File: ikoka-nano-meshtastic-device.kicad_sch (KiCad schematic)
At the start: 8 parts, among them J1 Battery, J2 Solar, J3 Qwiic_RA, Q1 FDN302P, U1 Seeed Studio XIAO nRF52840, U2 E22-900M30S

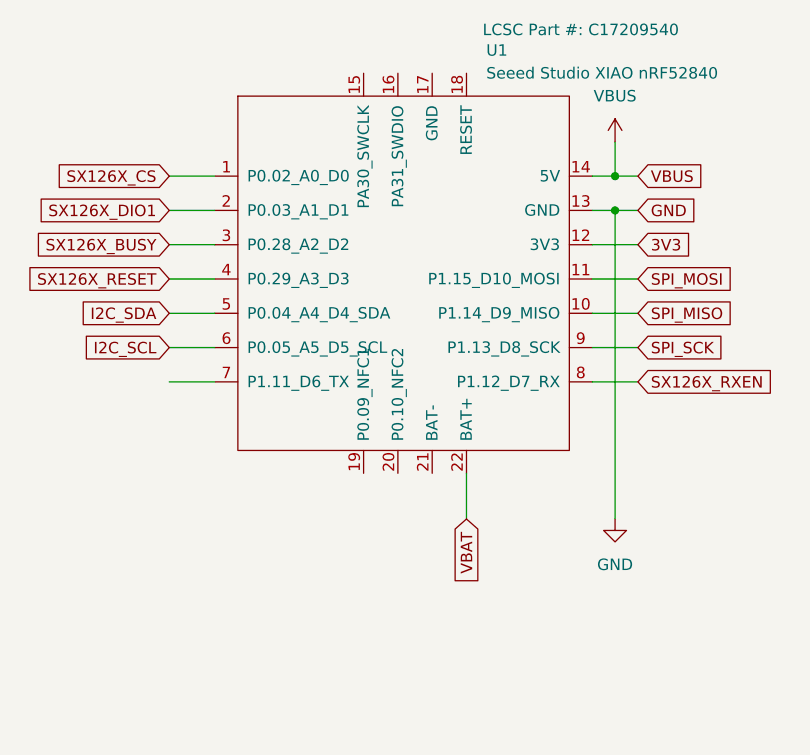
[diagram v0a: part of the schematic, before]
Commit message: Rebase XIAO BLE hand soldering symbol/footprint on upstream
Signed-off-by: Andrew Yong <me@ndoo.sg>
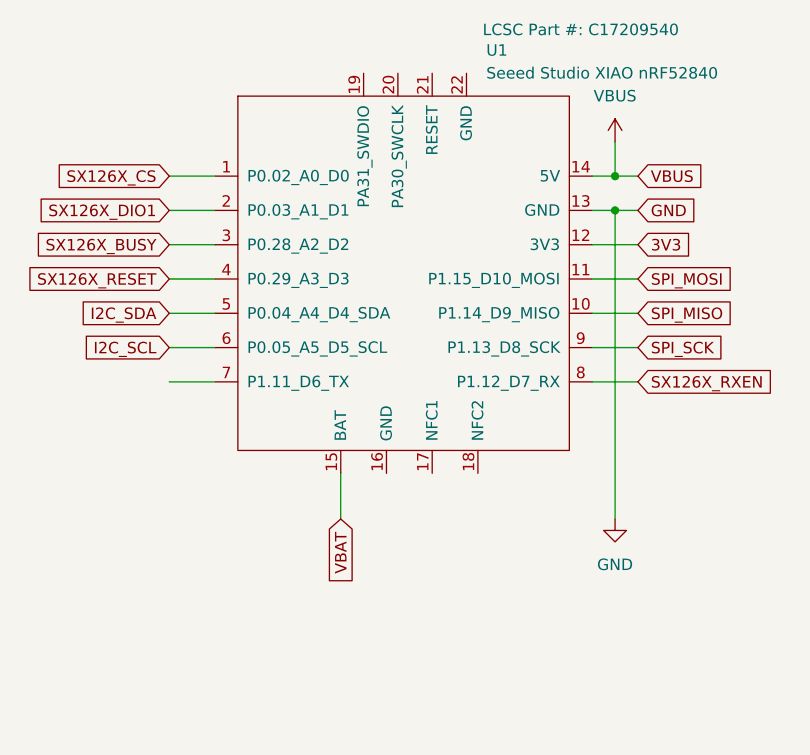
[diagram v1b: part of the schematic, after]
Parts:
- U1: footprint Seeed Studio XIAO Series Library:XIAO-nRF52840-BatteryPTH-14P-2.54-21X17.8MM -> Seeed Studio XIAO Series Library:XIAO-nRF52840-SMD_Handsoldering; symbol Seeed_Studio_XIAO_Series:Seeed Studio XIAO nRF52840 -> Seeed_Studio_XIAO_Series:XIAO-nRF52840-SMD
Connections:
- net VBAT: now also U1.15 (BAT); no longer U1.22 (BAT+)
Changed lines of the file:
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@@
 	(wire
 		(pts
-			(xy 87.63 81.28) (xy 87.63 86.36)
+			(xy 73.66 81.28) (xy 73.66 86.36)
 		)
 		(stroke
@@
 	(global_label "VBAT"
 		(shape input)
-		(at 87.63 86.36 270)
+		(at 73.66 86.36 270)
 		(fields_autoplaced yes)
 		(effects
@@
 		)
 		(property "Intersheetrefs" "${INTERSHEET_REFS}"
-			(at 87.63 93.76 90)
+			(at 73.66 93.76 90)
 			(effects
 				(font
@@
 	)
 	(symbol
-		(lib_id "Seeed_Studio_XIAO_Series:Seeed Studio XIAO nRF52840")
+		(lib_id "Seeed_Studio_XIAO_Series:XIAO-nRF52840-SMD")
 		(at 81.28 59.69 0)
 		(unit 1)
@@
 			)
 		)
-		(property "Footprint" "Seeed Studio XIAO Series Library:XIAO-nRF52840-BatteryPTH-14P-2.54-21X17.8MM"
+		(property "Footprint" "Seeed Studio XIAO Series Library:XIAO-nRF52840-SMD_Handsoldering"
 			(at 72.39 54.61 0)
 			(effects

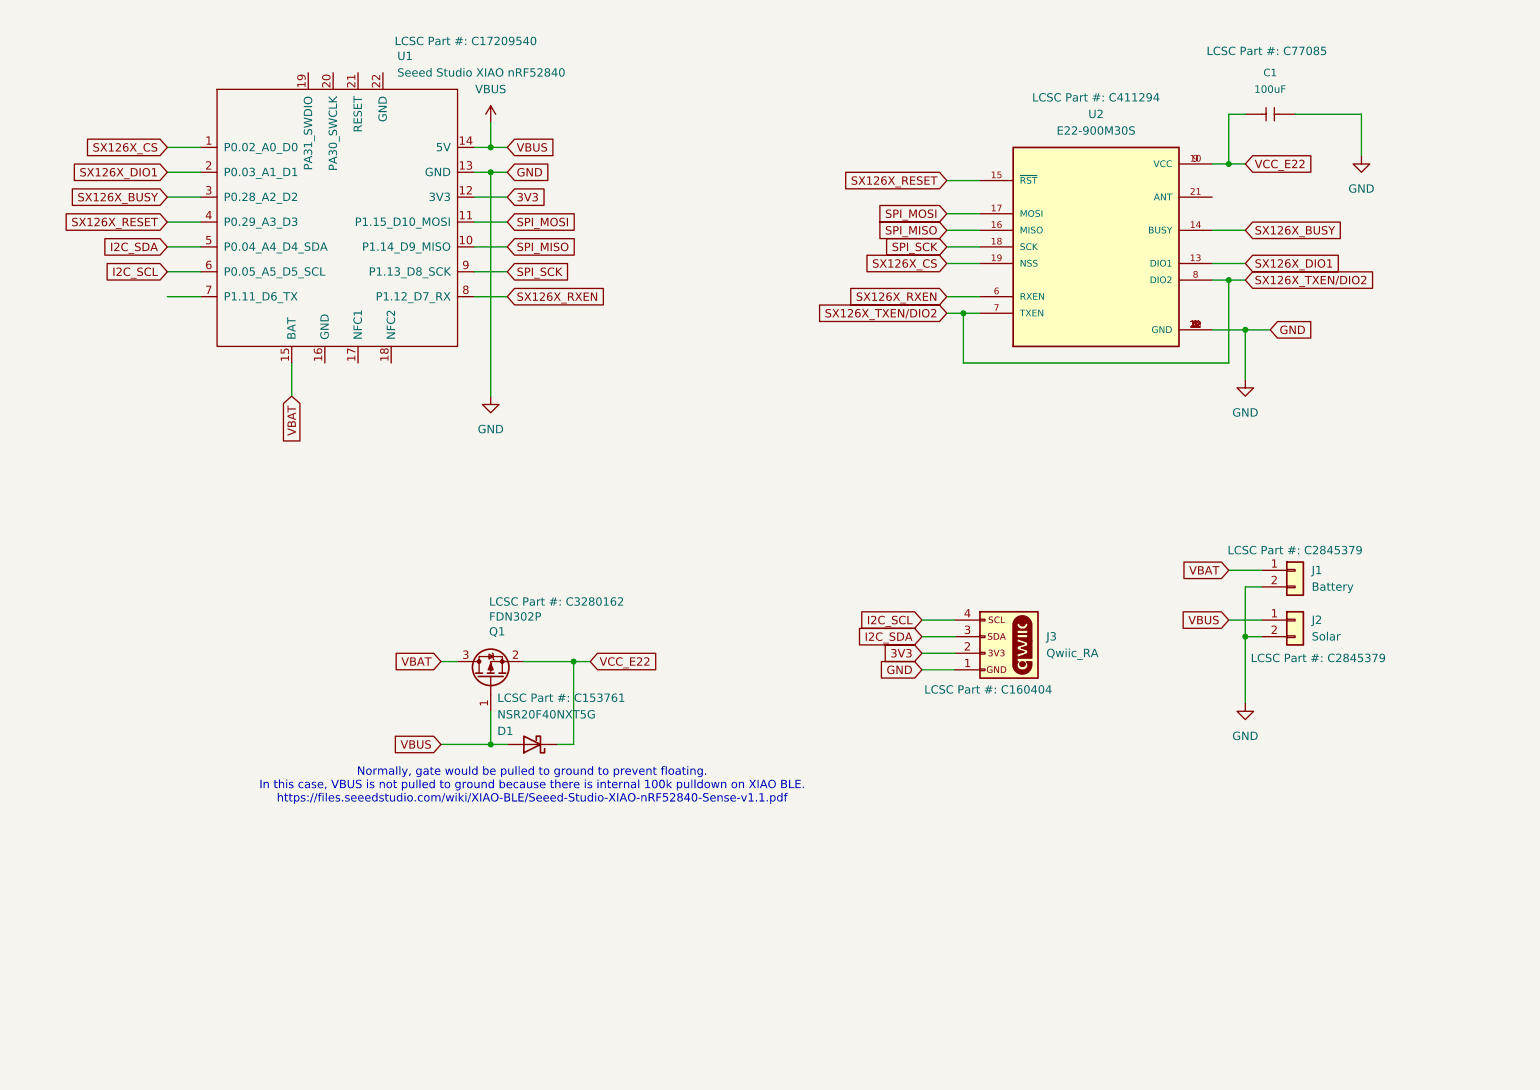
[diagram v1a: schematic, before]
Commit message: Add 5.4V boost converter circuit, use more JLCPCB basic parts, make PCB square, add internal battery connector
Signed-off-by: Andrew Yong <me@ndoo.sg>
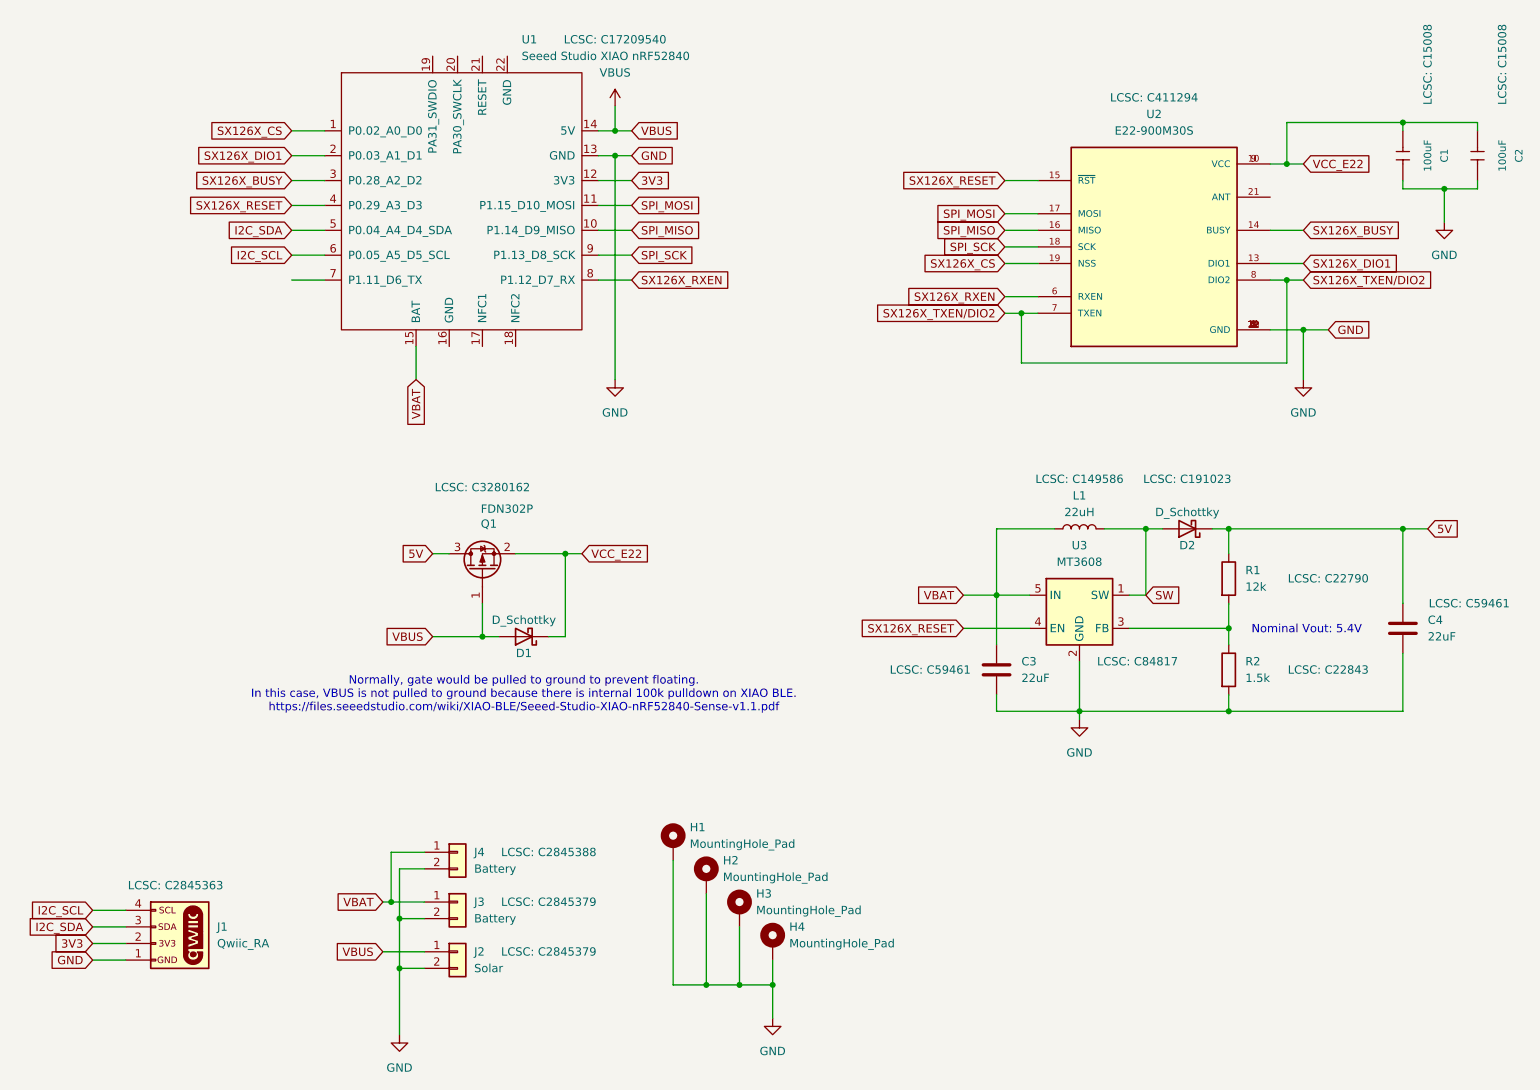
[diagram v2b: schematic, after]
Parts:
- added C2: 100uF, Capacitor_SMD:C_1206_3216Metric_Pad1.33x1.80mm_HandSolder, symbol OPL_Capacitor:CERAMIC-100UF-6.3V-20%-X5R_1206_
- added C3, C4: 22uF, Capacitor_SMD:C_0603_1608Metric_Pad1.08x0.95mm_HandSolder, symbol Device:C
- added D2: D_Schottky, Diode_SMD:D_SOD-323_HandSoldering, symbol Device:D_Schottky
- added H1, H2, H3, H4: MountingHole_Pad, MountingHole:MountingHole_2.7mm_M2.5_Pad_Via, symbol Mechanical:MountingHole_Pad
- added J4: Battery, Connector_Molex:Molex_PicoBlade_53398-0271_1x02-1MP_P1.25mm_Vertical, symbol Connector_Generic:Conn_01x02
- added L1: 22uH, Inductor_SMD:L_SXN_SMDRI64, symbol Device:L
- added R1: 12k, Resistor_SMD:R_0603_1608Metric_Pad0.98x0.95mm_HandSolder, symbol Device:R
- added R2: 1.5k, Resistor_SMD:R_0603_1608Metric_Pad0.98x0.95mm_HandSolder, symbol Device:R
- added U3: MT3608, Package_TO_SOT_SMD:SOT-23-6, symbol Regulator_Switching:MT3608
- C1: LCSC (none) -> C15008; LCSC Part # C77085 -> (none); MPN GRM31CR60J107ME39L -> CL31A107MQHNNNE; SKU 302010183 -> (none)
- D1: value NSR20F40NXT5G -> D_Schottky; footprint Diode_SMD:D_0603_1608Metric_Pad1.05x0.95mm_HandSolder -> Diode_SMD:D_SOD-323_HandSoldering; LCSC (none) -> C191023; LCSC Part # C153761 -> (none)
- J1: renamed from J3; LCSC (none) -> C2845363; LCSC Part # C160404 -> (none)
- J2: LCSC (none) -> C2845379; LCSC Part # C2845379 -> (none)
- J3: renamed from J1; LCSC (none) -> C2845379; LCSC Part # C2845379 -> (none)
- Q1: LCSC (none) -> C3280162; LCSC Part # C3280162 -> (none)
- U1: LCSC (none) -> C17209540; LCSC Part # C17209540 -> (none)
- U2: LCSC (none) -> C411294; LCSC Part # C411294 -> (none)
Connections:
- net GND: now also C2.1, C3.2, C4.2, H1.1, H2.1, H3.1, H4.1, J4.2 (Pin_2), R2.2, U3.2 (GND)
- net SX126X_RESET: now also U3.4 (EN)
- net VBAT: now also C3.1, J4.1 (Pin_1), L1.1, U3.5 (IN); no longer Q1.3 (D)
- net VCC_E22: now also C2.2
- new net: R1.2, R2.1, U3.3 (FB)
- new net 5V: C4.1, D2.1 (K), Q1.3 (D), R1.1
- new net SW: D2.2 (A), L1.2, U3.1 (SW)
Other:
- note added: "Nominal Vout: 5.4V"
- moved on the sheet: C1, D1, J1, J2, J3, Q1, U1, U2
